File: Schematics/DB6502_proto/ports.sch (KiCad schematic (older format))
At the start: 38 parts, among them J1 I/O Bus, J10 UART B, J2 System Bus, J3 Controls, J4 AVR ISP, J5 Debug UART, J6 USB A, J7 USB B, J8 Debug USB, J9 UART A

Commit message: Working on the second PCB
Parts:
- removed C10, C11: 10nF, Capacitor_THT:C_Disc_D5.0mm_W2.5mm_P2.50mm, symbol Device:C_Small
- removed C13, C14, C16, C17: 47pF, Capacitor_THT:C_Disc_D5.0mm_W2.5mm_P2.50mm, symbol Device:C_Small
- removed FB1, FB2: FB, Resistor_THT:R_Axial_DIN0207_L6.3mm_D2.5mm_P10.16mm_Horizontal, symbol Device:Ferrite_Bead_Small
- removed J6: USB A, Connector_USB:USB_B_OST_USB-B1HSxx_Horizontal, symbol 6502:USB_B
- removed J7: USB B, Connector_USB:USB_B_OST_USB-B1HSxx_Horizontal, symbol 6502:USB_B
- removed R12, R13, R14, R15: 27, Resistor_THT:R_Axial_DIN0207_L6.3mm_D2.5mm_P10.16mm_Horizontal, symbol Device:R
- added J12: Power plug, Connector_BarrelJack:BarrelJack_Horizontal, symbol Connector:Barrel_Jack
- renumbered C9 to C10, C12 to C11, C15 to C12, C18 to C13, FB3 to FB1, J3 to J1, J4 to J2, J8 to J3, J5 to J4, J9 to J5, J10 to J6, J1 to J7, J2 to J8, R8 to R10, R9 to R11, R10 to R12, R16 to R13, R17 to R14, R11 to R5, R4 to R6, R5 to R7, R6 to R8, R7 to R9
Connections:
- net labels removed: UART_A_USBD+, UART_A_USBD-, UART_B_USBD+, UART_B_USBD-
- wire segments 278 -> 233
- no-connect marks 4 -> 5

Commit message: Most chips placed, tracing continues
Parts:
- removed C11: 10nF, Capacitor_THT:C_Disc_D5.0mm_W2.5mm_P2.50mm, symbol Device:C_Small
- removed FB1: FB, Resistor_THT:R_Axial_DIN0207_L6.3mm_D2.5mm_P10.16mm_Horizontal, symbol Device:Ferrite_Bead_Small
- added R20: 4K7, Resistor_THT:R_Axial_DIN0207_L6.3mm_D2.5mm_P10.16mm_Horizontal, symbol Device:R
- added R21: 10K, Resistor_THT:R_Axial_DIN0207_L6.3mm_D2.5mm_P10.16mm_Horizontal, symbol Device:R
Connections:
- net labels added: VBUS_SENSE
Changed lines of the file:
@@
 $EndComp
 NoConn ~ 8350 4000
-$Comp
-L Device:Ferrite_Bead_Small FB1
-U 1 1 5FFE8733
-P 9300 3400
-AR Path="/6014B4D9/5FFE8733" Ref="FB1"  Part="1"
-AR Path="/5F8F4E1E/5FFE8733" Ref="FB?"  Part="1"
-F 0 "FB1" V 9063 3400 50  0000 C CNN
-F 1 "FB" V 9154 3400 50  0000 C CNN
-F 2 "Resistor_THT:R_Axial_DIN0207_L6.3mm_D2.5mm_P10.16mm_Horizontal" V 9230 3400 50  0001 C CNN
-F 3 "~" H 9300 3400 50  0001 C CNN
-	1    9300 3400
-	0    1    1    0
-$EndComp
-Text GLabel 10250 3400 2    50   Input ~ 0
-+5V
-Wire Wire Line
-	8750 3400 8950 3400
 Wire Wire Line
 	8750 3700 8850 3700
@@
 	9650 3850 9850 3850
 $Comp
-L Device:C_Small C11
-U 1 1 5FFE8765
-P 8950 4050
-AR Path="/6014B4D9/5FFE8765" Ref="C11"  Part="1"
-AR Path="/5F8F4E1E/5FFE8765" Ref="C?"  Part="1"
-F 0 "C11" H 9042 4096 50  0000 L CNN
-F 1 "10nF" H 9042 4005 50  0000 L CNN
-F 2 "Capacitor_THT:C_Disc_D5.0mm_W2.5mm_P2.50mm" H 8950 4050 50  0001 C CNN
-F 3 "~" H 8950 4050 50  0001 C CNN
-	1    8950 4050
-	1    0    0    -1
-$EndComp
-Wire Wire Line
-	8950 3950 8950 3400
-Connection ~ 8950 3400
-Wire Wire Line
-	8950 3400 9200 3400
-Wire Wire Line
-	8950 4250 8950 4150
-$Comp
 L Connector:AVR-ISP-6 J2
 U 1 1 600EABFA
@@
 Wire Wire Line
 	10250 4250 9650 4250
-Connection ~ 8950 4250
-Wire Wire Line
-	8950 4250 8450 4250
 Connection ~ 9300 4250
-Wire Wire Line
-	9300 4250 8950 4250
 Connection ~ 9650 4250
 Wire Wire Line
@@
 Wire Wire Line
 	8450 4000 8450 4250
-Wire Wire Line
-	9400 3400 10250 3400
 $Comp
 L Connector:Barrel_Jack J12
@@
 Wire Wire Line
 	8750 2750 8950 2750
-Wire Bus Line
-	7700 2600 7700 2800
-Wire Bus Line
-	2400 3650 2400 4050
-Wire Bus Line
-	4700 6700 5400 6700
-Wire Bus Line
-	2250 4150 2250 4850
-Wire Bus Line
-	4200 3250 4200 3950
-Wire Bus Line
-	3100 6700 4600 6700
 Text GLabel 4850 2750 0    50   Input ~ 0
 DBG_CLK
+Wire Wire Line
+	8450 4250 9300 4250
+$Comp
+L Device:R R20
+U 1 1 604AB578
+P 9000 3400
+F 0 "R20" V 8900 3400 50  0000 C CNN
+F 1 "4K7" V 9000 3400 50  0000 C CNN
+F 2 "Resistor_THT:R_Axial_DIN0207_L6.3mm_D2.5mm_P10.16mm_Horizontal" V 8930 3400 50  0001 C CNN
+F 3 "~" H 9000 3400 50  0001 C CNN
+	1    9000 3400
+	0    1    1    0
+$EndComp
+$Comp
+L Device:R R21
+U 1 1 604AC544
+P 9500 3400
+F 0 "R21" V 9400 3400 50  0000 C CNN
+F 1 "10K" V 9500 3400 50  0000 C CNN
+F 2 "Resistor_THT:R_Axial_DIN0207_L6.3mm_D2.5mm_P10.16mm_Horizontal" V 9430 3400 50  0001 C CNN
+F 3 "~" H 9500 3400 50  0001 C CNN
+	1    9500 3400
+	0    1    1    0
+$EndComp
+Text GLabel 10250 3400 2    50   Input ~ 0
+GND
+Wire Wire Line
+	9650 3400 10250 3400
+Wire Wire Line
+	9150 3400 9250 3400
+Wire Wire Line
+	8750 3400 8850 3400
+Text GLabel 10250 3250 2    50   Input ~ 0
+VBUS_SENSE
+Wire Wire Line
+	10250 3250 9250 3250
+Wire Wire Line
+	9250 3250 9250 3400
+Wire Bus Line
+	7700 2600 7700 2800
+Wire Bus Line
+	2400 3650 2400 4050
+Wire Bus Line
+	4700 6700 5400 6700
+Wire Bus Line
+	2250 4150 2250 4850
+Wire Bus Line
+	4200 3250 4200 3950
+Wire Bus Line
+	3100 6700 4600 6700
+Connection ~ 9250 3400
+Wire Wire Line
+	9250 3400 9350 3400
 $EndSCHEMATC

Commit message: Updates and fixes
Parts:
- removed R11, R6, R9: 4K7, Resistor_THT:R_Axial_DIN0207_L6.3mm_D2.5mm_P10.16mm_Horizontal, symbol Device:R
- J1, J7: footprint Connector_PinSocket_2.54mm:PinSocket_1x32_P2.54mm_Vertical -> Connector_PinSocket_2.54mm:PinSocket_1x40_P2.54mm_Vertical; symbol Connector:Conn_01x32_Female -> Connector:Conn_01x40_Female
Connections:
- net CLK is gone; now on net ~6502_RES: J7.27 (Pin_27)
- net SR_CLK is gone; now on net EXRAM: J1.15 (Pin_15)
- net SR_DAT is gone; now on net R~W: J1.14 (Pin_14)
- net +5V: now also J1.1 (Pin_1), J1.39 (Pin_39), J7.1 (Pin_1), J7.39 (Pin_39); no longer J1.31 (Pin_31), J7.31 (Pin_31)
- net 6502_CLK: now also J1.13 (Pin_13), J7.29 (Pin_29); no longer J1.11 (Pin_11)
- net 6502_RDY: now also J1.24 (Pin_24), J1.7 (Pin_7); no longer J1.22 (Pin_22), J1.5 (Pin_5)
- net BE: now also J1.8 (Pin_8); no longer J1.6 (Pin_6)
- net DBG_CLK: now also J1.19 (Pin_19); no longer J1.17 (Pin_17)
- net DBG_WAIT: now also J1.23 (Pin_23); no longer J1.21 (Pin_21)
- net EXRAM: no longer J1.13 (Pin_13)
- net GND: now also J1.2 (Pin_2), J1.40 (Pin_40), J7.2 (Pin_2), J7.40 (Pin_40); no longer J1.32 (Pin_32), J7.32 (Pin_32)
- net IOCS: now also J7.16 (Pin_16); no longer J7.14 (Pin_14)
- net RAM1_~CS: now also J7.30 (Pin_30); no longer J7.28 (Pin_28)
- net RAM2_~CS: now also J7.31 (Pin_31); no longer J7.29 (Pin_29)
- net RDY_M1F: now also J1.20 (Pin_20); no longer J1.18 (Pin_18)
- net RDY_M2F: now also J1.21 (Pin_21); no longer J1.19 (Pin_19)
- net ROM_~CS: now also J7.32 (Pin_32); no longer J7.30 (Pin_30)
- net R~W: now also J7.28 (Pin_28); no longer J1.12 (Pin_12), J7.26 (Pin_26)
- net SYNC: now also J1.4 (Pin_4); no longer J1.2 (Pin_2)
- net WS_DISABLE: now also J1.22 (Pin_22); no longer J1.20 (Pin_20)
- net a0: now also J7.3 (Pin_3); no longer J7.1 (Pin_1)
- net a1: now also J7.4 (Pin_4); no longer J7.2 (Pin_2)
- net a2: now also J7.5 (Pin_5); no longer J7.3 (Pin_3)
- net a3: now also J7.6 (Pin_6); no longer J7.4 (Pin_4)
- net a4: now also J7.7 (Pin_7); no longer J7.5 (Pin_5)
- net d0: now also J1.25 (Pin_25), J7.8 (Pin_8); no longer J1.23 (Pin_23), J7.6 (Pin_6)
- net d1: now also J1.26 (Pin_26), J7.9 (Pin_9); no longer J1.24 (Pin_24), J7.7 (Pin_7)
- net d2: now also J1.27 (Pin_27), J7.10 (Pin_10); no longer J1.25 (Pin_25), J7.8 (Pin_8)
- net d3: now also J1.28 (Pin_28), J7.11 (Pin_11); no longer J1.26 (Pin_26), J7.9 (Pin_9)
- net d4: now also J1.29 (Pin_29), J7.12 (Pin_12); no longer J1.27 (Pin_27), J7.10 (Pin_10)
- net d5: now also J1.30 (Pin_30), J7.13 (Pin_13); no longer J1.28 (Pin_28), J7.11 (Pin_11)
- net d6: now also J1.31 (Pin_31), J7.14 (Pin_14); no longer J1.29 (Pin_29), J7.12 (Pin_12)
- net d7: now also J1.32 (Pin_32), J7.15 (Pin_15); no longer J1.30 (Pin_30), J7.13 (Pin_13)
- net ~6502_RES: now also J1.12 (Pin_12); no longer J1.10 (Pin_10), J7.25 (Pin_25)
- net ~IOCS0: now also J7.21 (Pin_21); no longer J7.19 (Pin_19)
- net ~IOCS1: now also J7.22 (Pin_22); no longer J7.20 (Pin_20)
- net ~IOCS2: now also J7.23 (Pin_23); no longer J7.21 (Pin_21)
- net ~IOCS3: now also J7.24 (Pin_24); no longer J7.22 (Pin_22)
- net ~IRQ: now also J1.9 (Pin_9); no longer J1.7 (Pin_7)
- net ~LATCH: now also J7.17 (Pin_17); no longer J7.15 (Pin_15)
- net ~ML: now also J1.5 (Pin_5); no longer J1.3 (Pin_3)
- net ~NMI: now also J1.10 (Pin_10); no longer J1.8 (Pin_8)
- net ~RD: now also J7.25 (Pin_25); no longer J7.23 (Pin_23)
- net ~RES: now also J1.3 (Pin_3); no longer J1.1 (Pin_1)
- net ~SO: now also J1.11 (Pin_11); no longer J1.9 (Pin_9)
- net ~UART: now also J7.20 (Pin_20); no longer J7.18 (Pin_18)
- net ~VIA1: now also J7.18 (Pin_18); no longer J7.16 (Pin_16)
- net ~VIA2: now also J7.19 (Pin_19); no longer J7.17 (Pin_17)
- net ~VP: now also J1.6 (Pin_6); no longer J1.4 (Pin_4)
- net ~WR: now also J7.26 (Pin_26); no longer J7.24 (Pin_24)
- net SR_OUT: no longer names the net of J1.16 (Pin_16)
- new net ~EXT_IRQ: J7.34 (Pin_34)
- new net ~VIA2_IRQ: J7.33 (Pin_33)

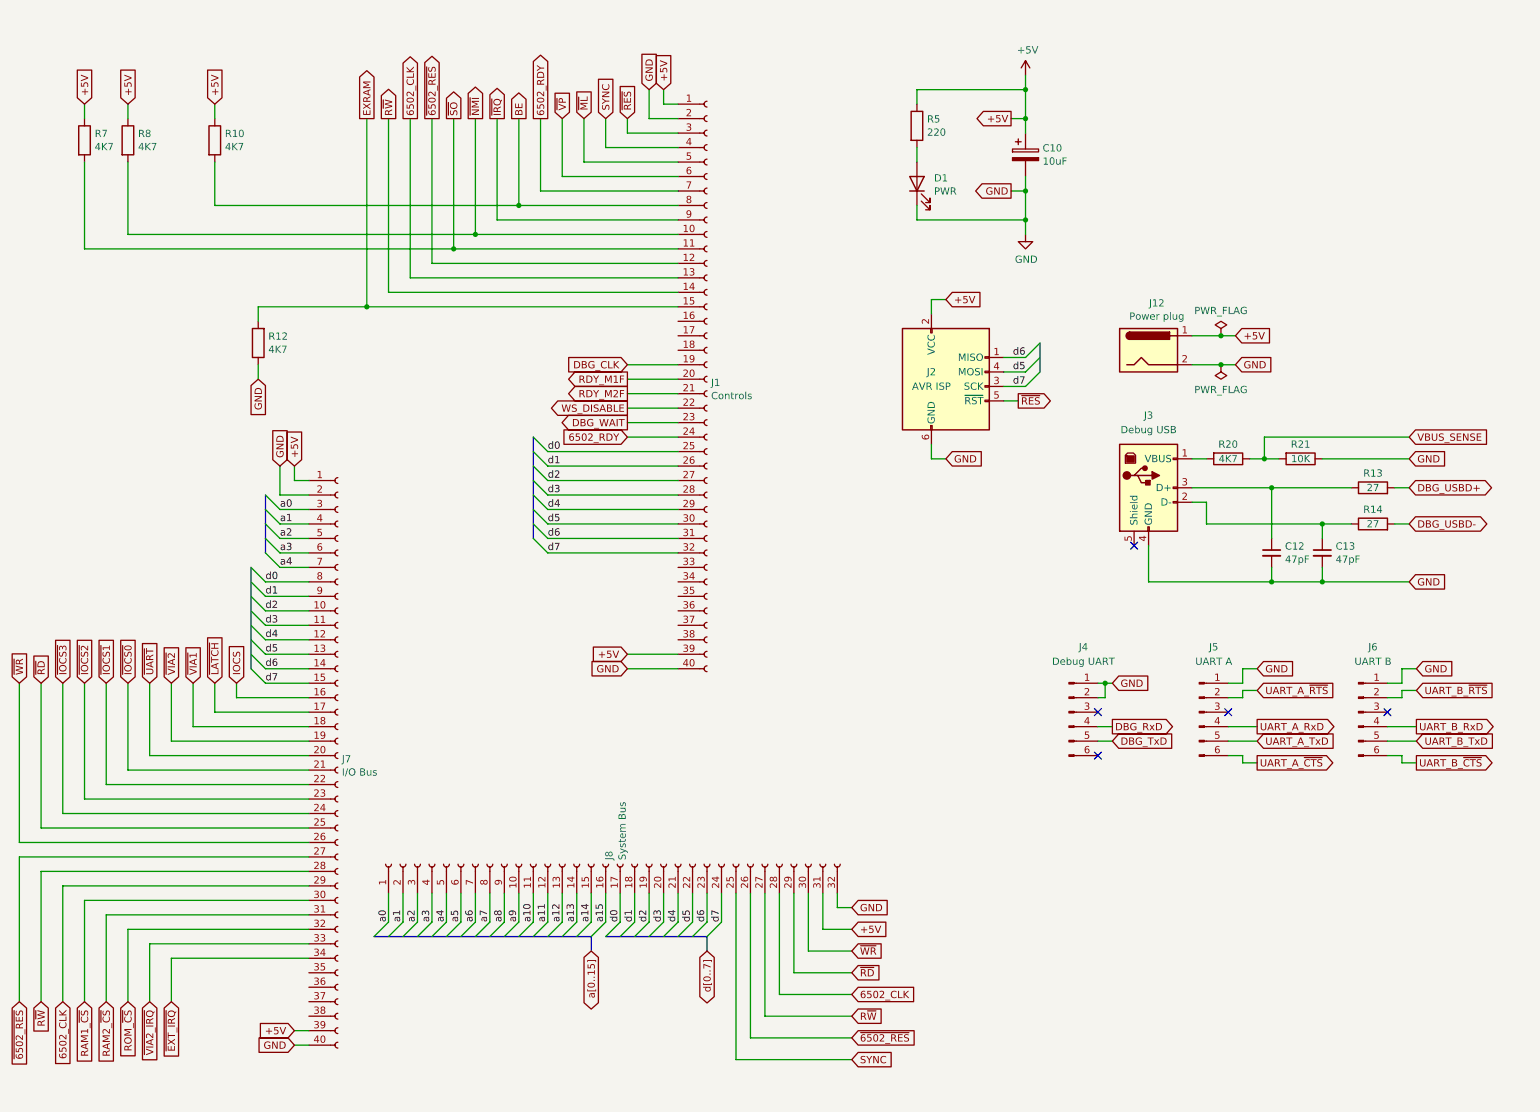
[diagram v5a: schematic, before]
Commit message: Redesigned jumpers, introduced resistor network
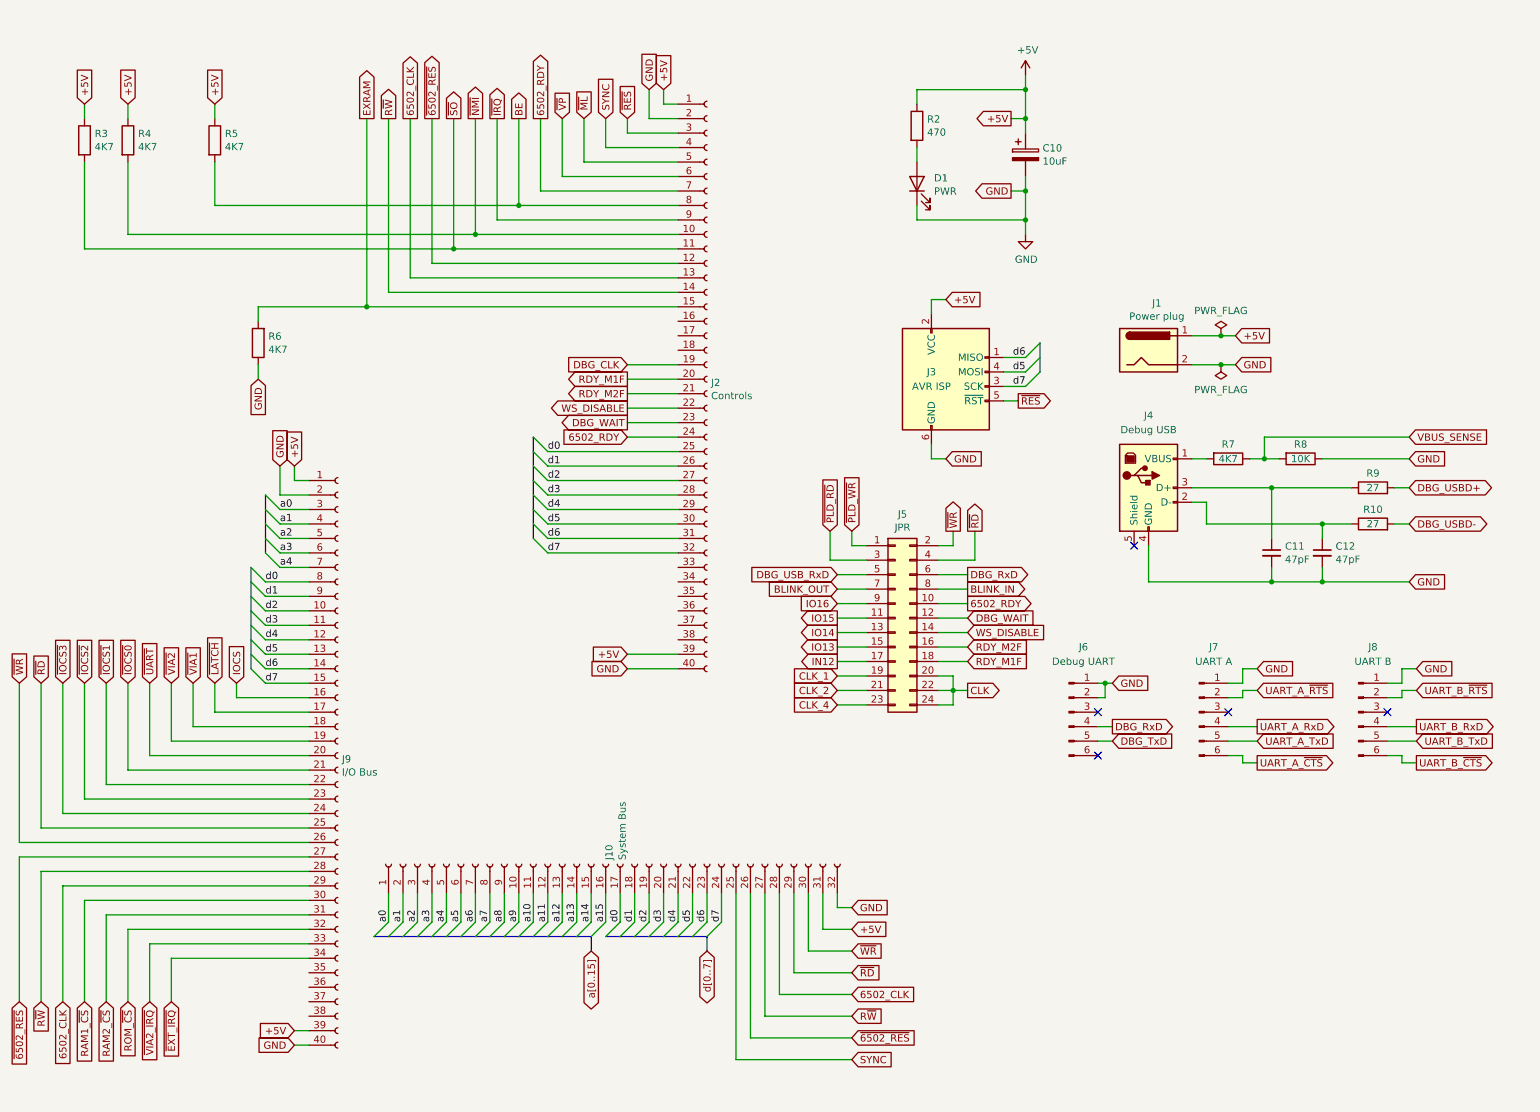
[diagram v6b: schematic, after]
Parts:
- added J5: JPR, Connector_PinHeader_2.54mm:PinHeader_2x12_P2.54mm_Vertical, symbol Connector_Generic:Conn_02x12_Odd_Even
- R2: renamed from R5; value 220 -> 470
- renumbered C12 to C11, C13 to C12, J12 to J1, J8 to J10, J1 to J2, J2 to J3, J3 to J4, J4 to J6, J5 to J7, J6 to J8, J7 to J9, R14 to R10, R7 to R3, R8 to R4, R10 to R5, R12 to R6, R20 to R7, R21 to R8, R13 to R9
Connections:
- net 6502_RDY: now also J5.10 (Pin_10)
- net DBG_RxD: now also J5.6 (Pin_6)
- net DBG_WAIT: now also J5.12 (Pin_12)
- net RDY_M1F: now also J5.18 (Pin_18)
- net RDY_M2F: now also J5.16 (Pin_16)
- net WS_DISABLE: now also J5.14 (Pin_14)
- net ~RD: now also J5.4 (Pin_4)
- net ~WR: now also J5.2 (Pin_2)
- new net BLINK_IN: J5.8 (Pin_8)
- new net BLINK_OUT: J5.7 (Pin_7)
- new net CLK: J5.20 (Pin_20), J5.22 (Pin_22), J5.24 (Pin_24)
- new net CLK_1: J5.19 (Pin_19)
- new net CLK_2: J5.21 (Pin_21)
- new net CLK_4: J5.23 (Pin_23)
- new net DBG_USB_RxD: J5.5 (Pin_5)
- new net IN12: J5.17 (Pin_17)
- new net IO13: J5.15 (Pin_15)
- new net IO14: J5.13 (Pin_13)
- new net IO15: J5.11 (Pin_11)
- new net IO16: J5.9 (Pin_9)
- new net ~PLD_RD: J5.3 (Pin_3)
- new net ~PLD_WR: J5.1 (Pin_1)

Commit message: Some schematic updates for new port layout
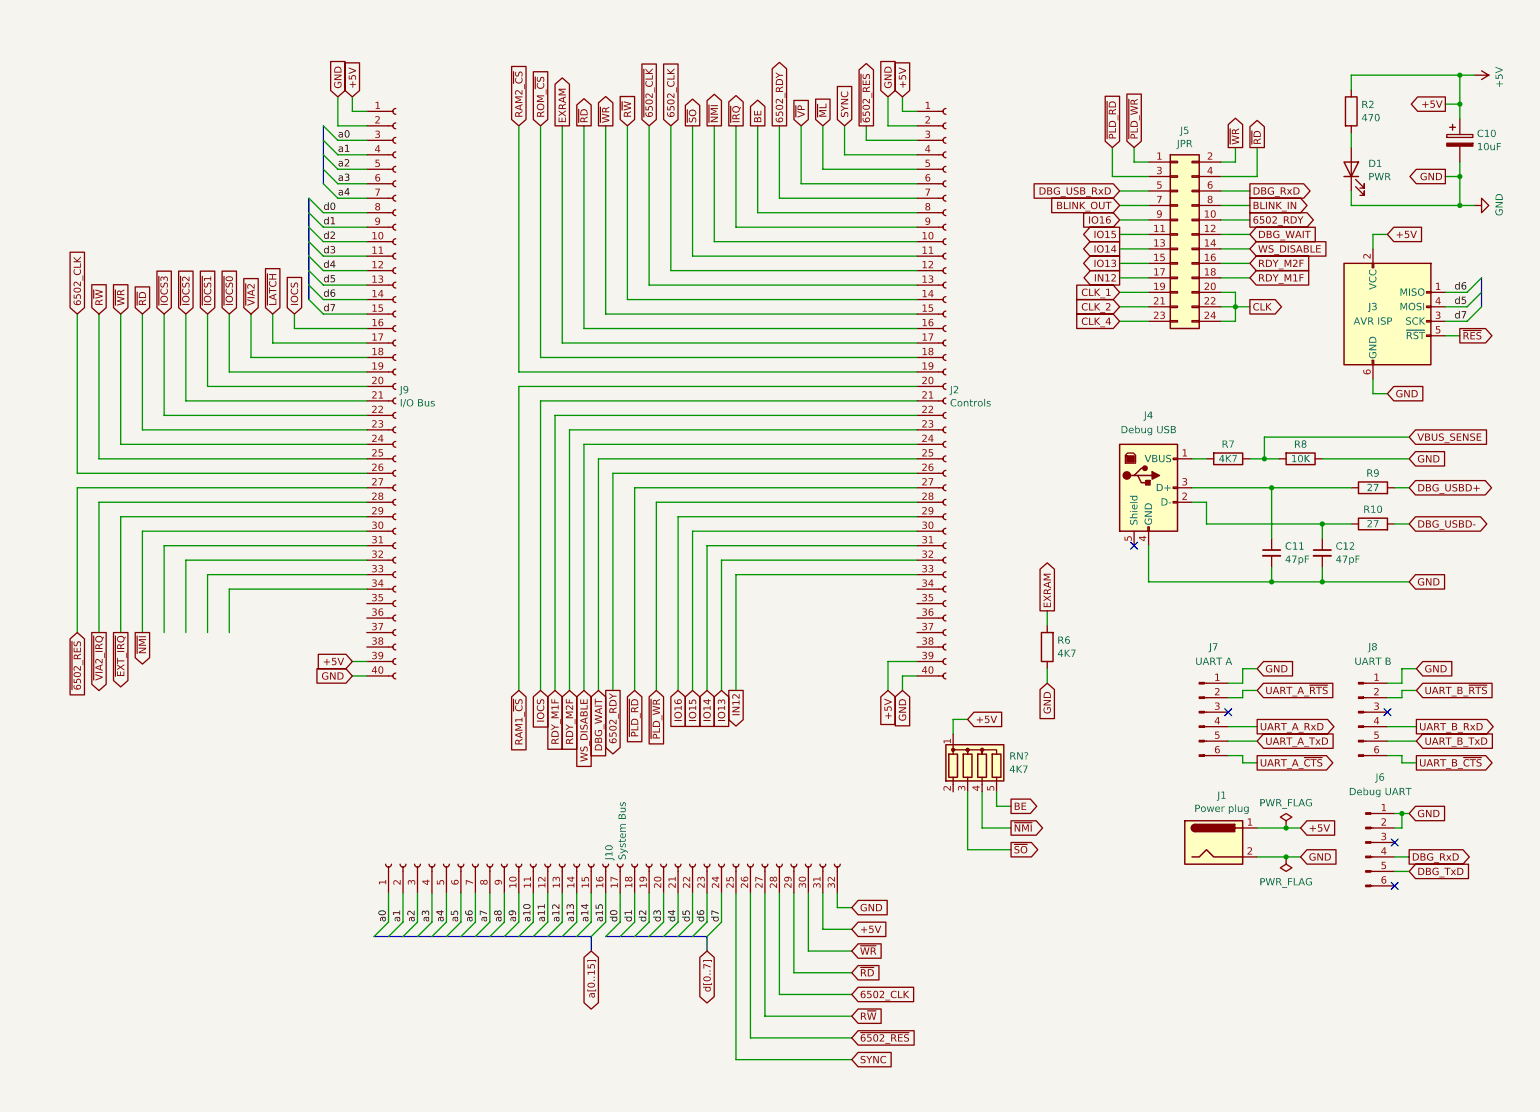
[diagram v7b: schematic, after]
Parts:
- removed R3, R4, R5: 4K7, Resistor_THT:R_Axial_DIN0207_L6.3mm_D2.5mm_P10.16mm_Horizontal, symbol Device:R
- added RN?: 4K7, Resistor_THT:R_Array_SIP5, symbol Device:R_Network04
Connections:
- net DBG_CLK is gone; now on net RAM2_~CS: J2.19 (Pin_19)
- net ~UART is gone; now on net ~IOCS1: J9.20 (Pin_20)
- net ~VIA1 is gone; now on net ~VIA2: J9.18 (Pin_18)
- net +5V: now also RN?.1 (common)
- net 6502_CLK: now also J2.12 (Pin_12), J9.26 (Pin_26); no longer J2.13 (Pin_13), J9.29 (Pin_29)
- net 6502_RDY: now also J2.26 (Pin_26); no longer J2.24 (Pin_24)
- net BE: now also RN?.5 (R4)
- net DBG_WAIT: now also J2.25 (Pin_25); no longer J2.23 (Pin_23)
- net EXRAM: now also J2.17 (Pin_17); no longer J2.15 (Pin_15)
- net IN12: now also J2.33 (Pin_33)
- net IO13: now also J2.32 (Pin_32)
- net IO14: now also J2.31 (Pin_31)
- net IO15: now also J2.30 (Pin_30)
- net IO16: now also J2.29 (Pin_29)
- net IOCS: now also J2.21 (Pin_21)
- net RAM1_~CS: now also J2.20 (Pin_20); no longer J9.30 (Pin_30)
- net RAM2_~CS: no longer J9.31 (Pin_31)
- net RDY_M1F: now also J2.22 (Pin_22); no longer J2.20 (Pin_20)
- net RDY_M2F: now also J2.23 (Pin_23); no longer J2.21 (Pin_21)
- net ROM_~CS: now also J2.18 (Pin_18); no longer J9.32 (Pin_32)
- net R~W: now also J9.25 (Pin_25); no longer J9.28 (Pin_28)
- net WS_DISABLE: now also J2.24 (Pin_24); no longer J2.22 (Pin_22)
- net d0: no longer J2.25 (Pin_25)
- net d1: no longer J2.26 (Pin_26)
- net d2: no longer J2.27 (Pin_27)
- net d3: no longer J2.28 (Pin_28)
- net d4: no longer J2.29 (Pin_29)
- net d5: no longer J2.30 (Pin_30)
- net d6: no longer J2.31 (Pin_31)
- net d7: no longer J2.32 (Pin_32)
- net ~6502_RES: now also J2.3 (Pin_3); no longer J2.12 (Pin_12)
- net ~EXT_IRQ: now also J9.29 (Pin_29); no longer J9.34 (Pin_34)
- net ~IOCS0: now also J9.19 (Pin_19); no longer J9.21 (Pin_21)
- net ~IOCS1: no longer J9.22 (Pin_22)
- net ~IOCS2: now also J9.21 (Pin_21); no longer J9.23 (Pin_23)
- net ~IOCS3: now also J9.22 (Pin_22); no longer J9.24 (Pin_24)
- net ~NMI: now also J9.30 (Pin_30), RN?.4 (R3)
- net ~PLD_RD: now also J2.27 (Pin_27)
- net ~PLD_WR: now also J2.28 (Pin_28)
- net ~RD: now also J2.16 (Pin_16), J9.23 (Pin_23); no longer J9.25 (Pin_25)
- net ~RES: no longer J2.3 (Pin_3)
- net ~SO: now also RN?.3 (R2)
- net ~VIA2: no longer J9.19 (Pin_19)
- net ~VIA2_IRQ: now also J9.28 (Pin_28); no longer J9.33 (Pin_33)
- net ~WR: now also J2.15 (Pin_15), J9.24 (Pin_24); no longer J9.26 (Pin_26)
- new net ~6502_CLK: J2.13 (Pin_13)
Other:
- moved on the sheet: C10, D1, J1, J2, J3, J5, J6, J9, R2, R6
